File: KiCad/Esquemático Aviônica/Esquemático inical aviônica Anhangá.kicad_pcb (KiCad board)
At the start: 2 copper layers, 20 parts, among them J1 Conn_01x06_Female, J2 Conn_01x06_Female, J3 Conn_01x12_Female, J4 Conn_01x12_Female, J5 Screw_Terminal_01x02, J6 Conn_01x06_Male, J7 Screw_Terminal_01x02, J8 Conn_01x07_Female, Q1 IRF7403, U1 LD1117S18TR_SOT223

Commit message: Esquemático e Layout reformulados
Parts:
- J1, J2: footprint Connector_PinSocket_1.00mm:PinSocket_1x06_P1.00mm_Vertical -> Connector_PinSocket_2.54mm:PinSocket_1x06_P2.54mm_Vertical
- J3, J4: footprint Connector_PinSocket_1.00mm:PinSocket_1x12_P1.00mm_Vertical -> Connector_PinSocket_2.54mm:PinSocket_1x12_P2.54mm_Vertical
- J6: footprint Connector_PinHeader_1.00mm:PinHeader_1x06_P1.00mm_Vertical -> Connector_PinHeader_2.54mm:PinHeader_1x06_P2.54mm_Vertical
- J8: footprint Connector_PinHeader_1.00mm:PinHeader_1x07_P1.00mm_Vertical -> Connector_PinSocket_2.54mm:PinSocket_1x07_P2.54mm_Vertical
- R1, R2, R3, R4, R5: footprint Resistor_THT:R_Axial_DIN0204_L3.6mm_D1.6mm_P5.08mm_Horizontal -> Resistor_SMD:R_0805_2012Metric_Pad1.15x1.40mm_HandSolder; moved to B.Cu
- U1: value LD1117S18TR_SOT223 -> ME620933
- moved J7 62.7 mm to (134.0, 77.5), turned to 90 degrees
- moved BZ1 48.5 mm to (99.7, 142.9), turned to 0 degrees
- moved J4 44.8 mm to (127.0, 66.0), turned to 0 degrees
- moved D1 37.9 mm to (135.3, 95.2), turned to 180 degrees
- moved U1 35.0 mm to (135.6, 103.7)
- moved C3 29.4 mm to (121.3, 86.9), turned to 0 degrees
- moved R1 28.6 mm to (122.6, 76.4), turned to 270 degrees
- moved J8 26.2 mm to (121.9, 148.0), turned to 90 degrees
- moved J3 24.6 mm to (111.8, 94.0), turned to 180 degrees
- moved R4 24.3 mm to (123.8, 83.6), turned to 270 degrees
- moved R2 22.6 mm to (121.3, 73.7), turned to 0 degrees
- moved J2 21.8 mm to (113.3, 96.4), turned to 90 degrees
- moved R5 18.1 mm to (116.3, 86.9)
- moved Q1 16.8 mm to (118.7, 80.0), turned to 90 degrees
- moved R3 16.2 mm to (133.7, 91.4), turned to 180 degrees
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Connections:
- BZ1 pad 1: D2 -> D8
- J4 pad 2: D_OUTPUT_NÍQUEL -> D8
- J4 pad 3: D7 -> (no net)
- J4 pad 4: D6 -> (no net)
- J8 pad 1: D7 -> GND
- J8 pad 2: D6 -> GND
- R4 pad 2: D_OUTPUT_NÍQUEL -> D2
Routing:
- net VCC: track 0.00 -> 88.9 mm, vias 0 -> 2
- net CS: track 0.00 -> 76.4 mm
- net VBAT: track 158.7 -> 86.6 mm, vias 0 -> 2
- net SCK: track 0.00 -> 70.6 mm
- net RXD0: track 0.00 -> 58.1 mm
- net RXD: track 0.00 -> 54.7 mm
- net MOSI: track 0.00 -> 52.5 mm
- net MISO: track 0.00 -> 47.0 mm
- net ANAL_INPUT_V_NÍQUEL: track 42.6 -> 7.68 mm
- net Net-(C3-Pad1): track 34.6 -> 17.3 mm
- net +3V3: track 9.24 -> 25.2 mm
- net SDA: track 0.00 -> 6.35 mm
- net SCL: track 0.00 -> 6.35 mm
- net Net-(D1-Pad2): track 34.8 -> 38.6 mm, vias 0 -> 2
- net D2: track 0.00 -> 3.56 mm
- added copper zone on B.Cu, net GND
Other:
- board outline added: 65 x 90 mm

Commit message: Atualização do Layout
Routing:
- net D8: track 0.00 -> 123.1 mm
- net MOSI: track 52.5 -> 45.7 mm
- net SCK: track 70.6 -> 64.0 mm
- net CS: track 76.4 -> 69.9 mm
- net MISO: track 47.0 -> 41.3 mm

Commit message: Revisão pós montagem
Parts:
- J5, J7: footprint TerminalBlock_4Ucon:TerminalBlock_4Ucon_1x02_P3.50mm_Horizontal -> TerminalBlock:TerminalBlock_bornier-2_P5.08mm
- moved J2 12.7 mm to (126.0, 96.4), turned to 270 degrees
- moved J5 6.90 mm to (135.2, 77.0)
- moved J7 6.49 mm to (135.1, 71.1)
- moved D1 3.99 mm to (131.4, 96.3), turned to 90 degrees
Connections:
- C1 pad 1: VCC -> +3V3
- J6 pad 1: VCC -> +3V3
- J8 pad 6: VCC -> +3V3
- U1 pad 3: VCC -> +3V3
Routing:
- net +3V3: track 25.2 -> 145.6 mm, vias 0 -> 2
- net VCC: track 88.9 -> 0.00 mm, vias 2 -> 0
- net RST: track 0.00 -> 15.2 mm
- net VBAT: track 86.6 -> 99.8 mm
- net Net-(D1-Pad2): track 38.6 -> 44.6 mm, vias 2 -> 3

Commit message: Adicionando novo BMP280
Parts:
- added J9: Conn_01x06_Male, Connector_PinHeader_2.54mm:PinHeader_1x06_P2.54mm_Vertical, F.Cu at (116.4, 137.4)
- C1, C2, C3: footprint Capacitor_SMD:C_0805_2012Metric_Pad1.15x1.40mm_HandSolder -> Capacitor_THT:C_Disc_D5.0mm_W2.5mm_P2.50mm
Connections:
- J3 pad 5: SCL -> SCL1
- J3 pad 6: SDA -> SDA1
- J3 pad 7: (no net) -> SCL2
- J3 pad 8: (no net) -> SDA2
- J6 pad 3: SCL -> SCL2
- J6 pad 4: SDA -> SDA2
- J6 pad 5: (no net) -> CSB
- J6 pad 6: (no net) -> SDO
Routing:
- net SDA: track 6.35 -> 0.00 mm
- net SCL: track 6.35 -> 0.00 mm

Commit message: Atualização Layout
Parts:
- J8: value Conn_01x07_Female -> Conn_01x02_Female; footprint Connector_PinSocket_2.54mm:PinSocket_1x07_P2.54mm_Vertical -> Connector_PinSocket_2.54mm:PinSocket_1x02_P2.54mm_Vertical
- R1, R2, R3, R4, R5: footprint Resistor_SMD:R_0805_2012Metric_Pad1.15x1.40mm_HandSolder -> Resistor_THT:R_Axial_DIN0207_L6.3mm_D2.5mm_P5.08mm_Vertical
- moved BZ1 58.9 mm to (95.8, 84.1), turned to 90 degrees
- moved J8 46.2 mm to (112.3, 102.9), turned to 0 degrees
- moved J1 43.5 mm to (96.5, 144.5), turned to 90 degrees
- moved J6 22.8 mm to (100.1, 111.3)
- moved J2 20.5 mm to (122.9, 116.7)
- moved J3 20.5 mm to (108.7, 114.3)
- moved J4 20.5 mm to (124.0, 86.4)
- moved R1 18.7 mm to (104.6, 71.1)
- moved R5 17.5 mm to (108.7, 71.1), turned to 270 degrees
- moved R4 16.3 mm to (113.3, 71.1)
- moved R2 10.6 mm to (112.8, 67.3), turned to 180 degrees
- moved J5 9.57 mm to (136.7, 67.6), turned to 180 degrees
- moved C3 9.01 mm to (115.8, 79.8)
- moved Q1 6.12 mm to (121.2, 74.4)
- moved J7 5.34 mm to (136.7, 76.2), turned to 180 degrees
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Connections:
- C1 pad 1: +3V3 -> VCC
- J1 pad 2: +3V3 -> VCC
- J2 pad 4: +3V3 -> 5V
- J3 pad 10: MISO -> MOSI
- J3 pad 11: MOSI -> MISO
- J3 pad 4: +3V3 -> 5V
- J3 pad 5: SCL1 -> (no net)
- J3 pad 6: SDA1 -> (no net)
- J3 pad 7: SCL2 -> (no net)
- J3 pad 8: SDA2 -> (no net)
- J4 pad 11: RXD0 -> (no net)
- J4 pad 12: RXD -> (no net)
- J6 pad 1: +3V3 -> VCC
- J6 pad 3: SCL2 -> SCL
- J6 pad 4: SDA2 -> SDA
- J6 pad 5: CSB -> VCC
- J6 pad 6: SDO -> VCC
- J8 pad 1: GND -> SDA
- J8 pad 2: GND -> SCL
- J9 pad 1: +3V3 -> VCC
- J9 pad 3: SCL1 -> SCL
- J9 pad 4: SDA1 -> SDA
- J9 pad 5: CSB -> VCC
- J9 pad 6: SDO -> GND
- U1 pad 3: +3V3 -> VCC
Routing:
- net VCC: track 0.00 -> 161.9 mm
- net SDA: track 0.00 -> 158.2 mm
- net +3V3: track 145.6 -> 0.00 mm, vias 2 -> 0
- net SCL: track 0.00 -> 96.1 mm, vias 0 -> 2
- net D8: track 123.1 -> 34.5 mm
- net RXD0: track 58.1 -> 0.00 mm
- net RXD: track 54.7 -> 0.00 mm
- net CS: track 69.9 -> 117.1 mm, vias 0 -> 2
- net ANAL_INPUT_V_NÍQUEL: track 7.68 -> 50.3 mm
- net D2: track 3.56 -> 42.7 mm
- net Net-(D1-Pad2): track 44.6 -> 70.8 mm, vias 3 -> 2
- net MISO: track 41.3 -> 61.3 mm
- net MOSI: track 45.7 -> 56.9 mm
- net SCK: track 64.0 -> 53.8 mm
- net GND: track 0.00 -> 2.54 mm
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
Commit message: Atualização Layout
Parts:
- C1, C3, R1, R2, R3, R4, R5: moved to F.Cu
- J6, J9: footprint Connector_PinHeader_2.54mm:PinHeader_1x06_P2.54mm_Vertical -> Connector_PinSocket_2.54mm:PinSocket_1x06_P2.54mm_Vertical

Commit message: Atual. Layout + Esquemát.
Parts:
- C2: moved to F.Cu
- moved J1 11.2 mm to (96.8, 133.3), turned to 0 degrees
- moved J9 8.29 mm to (124.5, 126.5)
- moved J7 7.45 mm to (134.2, 83.2), turned to 90 degrees
- moved C1 6.74 mm to (137.6, 100.9), turned to 90 degrees
- moved J5 4.58 mm to (132.3, 66.0), turned to 270 degrees
- moved U1 2.64 mm to (133.0, 104.2), turned to 270 degrees
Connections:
- J1 pad 2: VCC -> VBAT
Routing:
- net VCC: track 161.9 -> 104.7 mm, vias 0 -> 2
- net VBAT: track 101.0 -> 133.4 mm
- net SDA: track 158.2 -> 138.9 mm, vias 0 -> 2
- net CS: track 117.1 -> 102.1 mm, vias 2 -> 0
- net SCL: track 96.1 -> 103.7 mm
- net SCK: track 53.8 -> 60.3 mm
- net GND: track 2.54 -> 8.57 mm, vias 0 -> 2
- net MOSI: track 56.9 -> 59.9 mm
- net MISO: track 61.3 -> 60.0 mm
- net Net-(D1-Pad2): track 70.8 -> 71.3 mm, vias 2 -> 0

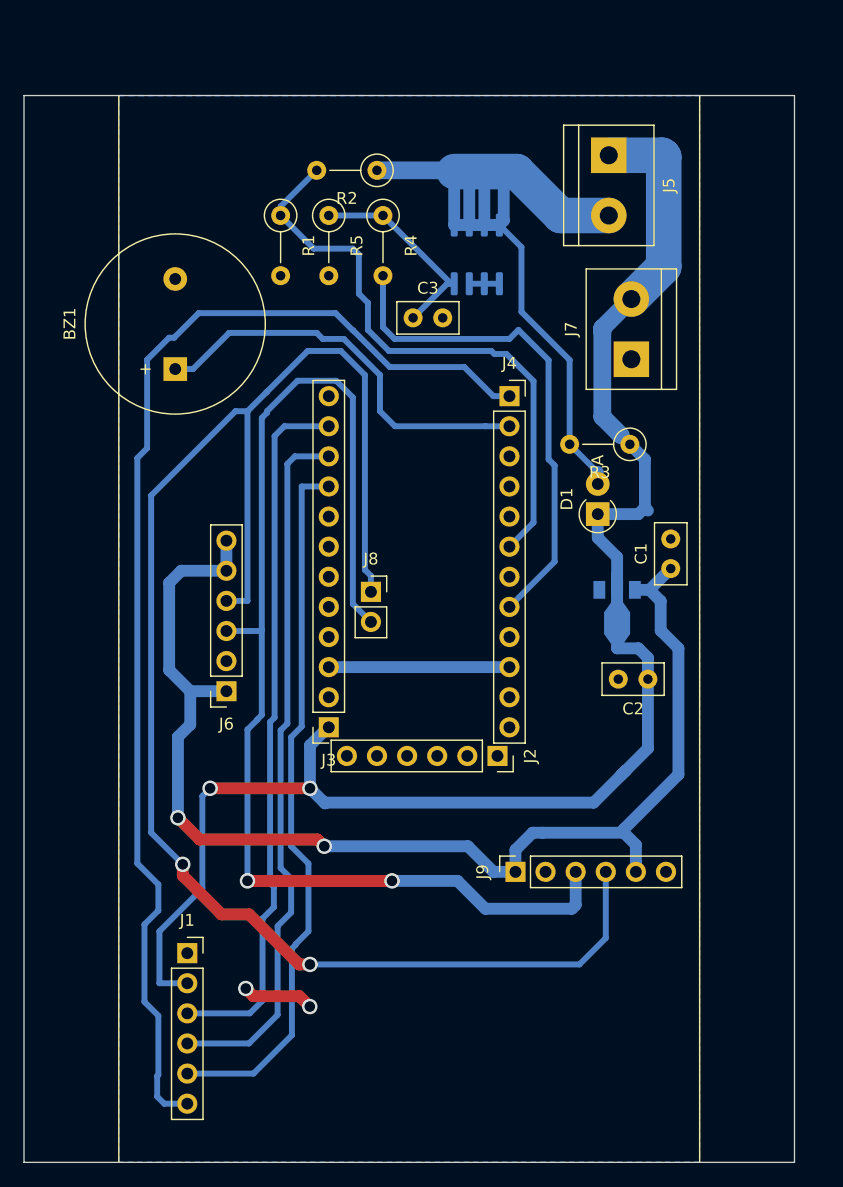
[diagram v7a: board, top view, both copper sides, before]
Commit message: Mudança de pinos
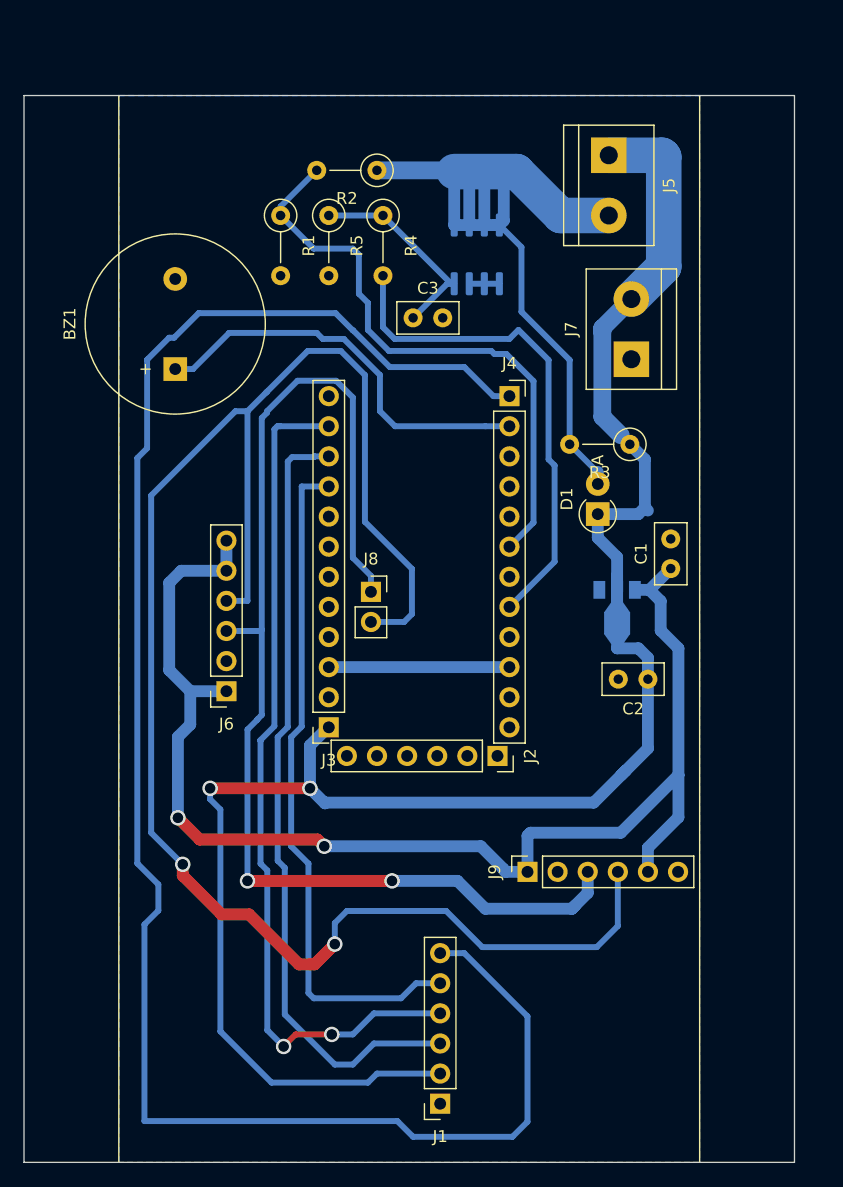
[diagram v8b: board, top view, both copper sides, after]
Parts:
- moved J1 24.8 mm to (118.1, 146.1), turned to 180 degrees
- moved J9 1.02 mm to (125.5, 126.5)
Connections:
- J3 pad 10: MOSI -> MISO
- J3 pad 11: MISO -> MOSI
- J8 pad 1: SDA -> SCL
- J8 pad 2: SCL -> SDA
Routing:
- net CS: track 102.1 -> 152.7 mm
- net VBAT: track 133.4 -> 154.4 mm
- net MOSI: track 59.9 -> 72.5 mm, vias 0 -> 2
- net SDA: track 138.9 -> 149.9 mm
- net MISO: track 60.0 -> 66.5 mm
- net VCC: track 104.7 -> 110.8 mm
- net GND: track 8.57 -> 2.54 mm, vias 2 -> 0
- net SCK: track 60.3 -> 57.8 mm
- net SCL: track 103.7 -> 102.1 mm
